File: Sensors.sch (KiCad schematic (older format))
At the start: 14 parts, among them Q20 2N7002K, Q21 2N7002K, U12 SHTC3, U13 M24C02-WDW

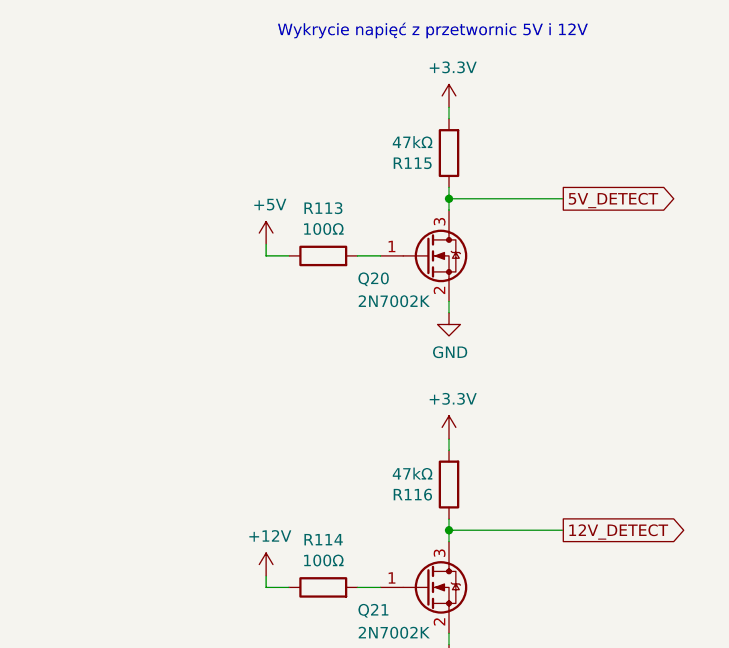
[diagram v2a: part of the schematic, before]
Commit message: Update elements value
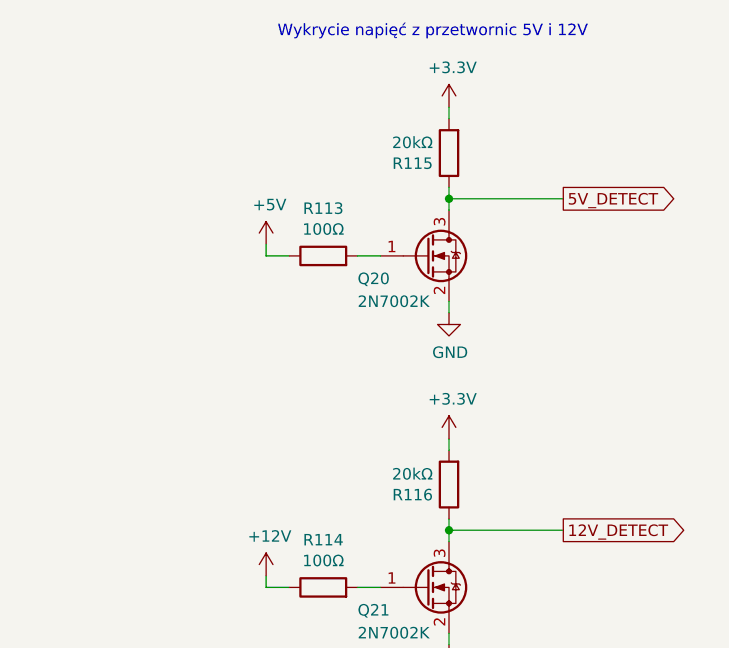
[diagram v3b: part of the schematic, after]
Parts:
- R1: Cena 0.04651 -> 0.03622
- R113, R114: Cena (none) -> 0.03185; Link (none) -> https://www.tme.eu/pl/details/smd0603-100r-1%25/rezystory-s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; Model (none) -> 0603SAF1000T5E; Opis (none) -> Rezystor: thick film; SMD; 0603; 100Ω; 0,1W; ±1%; -55÷155°C; Producent (none) -> ROYAL OHM; Typ (none) -> SMD
- R115, R116: value 47kΩ -> 20kΩ; Cena (none) -> 0.03572; Link (none) -> https://www.tme.eu/pl/details/smd0603-47k/rezystory-smd-060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; Model (none) -> 0603SAJ0473T5E; Opis (none) -> Rezystor: thick film; SMD; 0603; 47kΩ; 0,1W; ±5%; -55÷155°C; Producent (none) -> ROYAL OHM
- U13: Cena (none) -> 0.56; Link (none) -> https://pl.farnell.com/stmicroelectronics/m24c02-wdw6tp/eep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; Model (none) -> M24C02-WDW6TP; Opis (none) -> EEPROM, 2 Kbit, 256 x 8 bitów, Szeregowy I2C (2-Wire), 400 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; Producent (none) -> ST; Typ (none) -> SMD
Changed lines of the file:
@@
 AR Path="/5E1B3A8F/5E1CAE4C" Ref="R115"  Part="1"
 F 0 "R115" H 6920 1496 50  0000 L CNN
-F 1 "47kΩ" H 6920 1405 50  0000 L CNN
+F 1 "20kΩ" H 6920 1405 50  0000 L CNN
 F 2 "Resistor_SMD:R_0603_1608Metric" V 6780 1450 50  0001 C CNN
 F 3 "~" H 6850 1450 50  0001 C CNN
-F 4 "" H 6850 1450 50  0001 C CNN "Cena"
-F 5 "" H 6850 1450 50  0001 C CNN "Link"
-F 6 "" H 6850 1450 50  0001 C CNN "Model"
-F 7 "" H 6850 1450 50  0001 C CNN "Opis"
-F 8 "" H 6850 1450 50  0001 C CNN "Producent"
+F 4 "0.03572" H 6850 1450 50  0001 C CNN "Cena"
+F 5 "https://www.tme.eu/pl/details/smd0603-47k/rezystory-smd-0603/royal-ohm/0603saj0473t5e/" H 6850 1450 50  0001 C CNN "Link"
+F 6 "0603SAJ0473T5E" H 6850 1450 50  0001 C CNN "Model"
+F 7 "Rezystor: thick film; SMD; 0603; 47kΩ; 0,1W; ±5%; -55÷155°C" H 6850 1450 50  0001 C CNN "Opis"
+F 8 "ROYAL OHM" H 6850 1450 50  0001 C CNN "Producent"
 F 9 "SMD" H 6850 1450 50  0001 C CNN "Typ"
 	1    6850 1450
@@
 F 2 "Resistor_SMD:R_0603_1608Metric" V 6230 1900 50  0001 C CNN
 F 3 "~" H 6300 1900 50  0001 C CNN
+F 4 "0.03185" H 6300 1900 50  0001 C CNN "Cena"
+F 5 "https://www.tme.eu/pl/details/smd0603-100r-1%25/rezystory-smd-0603/royal-ohm/0603saf1000t5e/" H 6300 1900 50  0001 C CNN "Link"
+F 6 "0603SAF1000T5E" H 6300 1900 50  0001 C CNN "Model"
+F 7 "Rezystor: thick film; SMD; 0603; 100Ω; 0,1W; ±1%; -55÷155°C" H 6300 1900 50  0001 C CNN "Opis"
+F 8 "ROYAL OHM" H 6300 1900 50  0001 C CNN "Producent"
+F 9 "SMD" H 6300 1900 50  0001 C CNN "Typ"
 	1    6300 1900
 	0    -1   -1   0
@@
 AR Path="/5E1B3A8F/5E1DEF56" Ref="R116"  Part="1"
 F 0 "R116" H 6920 2946 50  0000 L CNN
-F 1 "47kΩ" H 6920 2855 50  0000 L CNN
+F 1 "20kΩ" H 6920 2855 50  0000 L CNN
 F 2 "Resistor_SMD:R_0603_1608Metric" V 6780 2900 50  0001 C CNN
 F 3 "~" H 6850 2900 50  0001 C CNN
-F 4 "" H 6850 2900 50  0001 C CNN "Cena"
-F 5 "" H 6850 2900 50  0001 C CNN "Link"
-F 6 "" H 6850 2900 50  0001 C CNN "Model"
-F 7 "" H 6850 2900 50  0001 C CNN "Opis"
-F 8 "" H 6850 2900 50  0001 C CNN "Producent"
+F 4 "0.03572" H 6850 2900 50  0001 C CNN "Cena"
+F 5 "https://www.tme.eu/pl/details/smd0603-47k/rezystory-smd-0603/royal-ohm/0603saj0473t5e/" H 6850 2900 50  0001 C CNN "Link"
+F 6 "0603SAJ0473T5E" H 6850 2900 50  0001 C CNN "Model"
+F 7 "Rezystor: thick film; SMD; 0603; 47kΩ; 0,1W; ±5%; -55÷155°C" H 6850 2900 50  0001 C CNN "Opis"
+F 8 "ROYAL OHM" H 6850 2900 50  0001 C CNN "Producent"
 F 9 "SMD" H 6850 2900 50  0001 C CNN "Typ"
 	1    6850 2900
@@
 F 2 "Resistor_SMD:R_0603_1608Metric" V 6230 3350 50  0001 C CNN
 F 3 "~" H 6300 3350 50  0001 C CNN
+F 4 "0.03185" H 6300 3350 50  0001 C CNN "Cena"
+F 5 "https://www.tme.eu/pl/details/smd0603-100r-1%25/rezystory-smd-0603/royal-ohm/0603saf1000t5e/" H 6300 3350 50  0001 C CNN "Link"
+F 6 "0603SAF1000T5E" H 6300 3350 50  0001 C CNN "Model"
+F 7 "Rezystor: thick film; SMD; 0603; 100Ω; 0,1W; ±1%; -55÷155°C" H 6300 3350 50  0001 C CNN "Opis"
+F 8 "ROYAL OHM" H 6300 3350 50  0001 C CNN "Producent"
+F 9 "SMD" H 6300 3350 50  0001 C CNN "Typ"
 	1    6300 3350
 	0    -1   -1   0
@@
 F 2 "Package_SO:TSSOP-8_4.4x3mm_P0.65mm" H 3550 4200 50  0001 C CNN
 F 3 "http://www.st.com/content/ccc/resource/technical/document/datasheet/b0/d8/50/40/5a/85/49/6f/DM00071904.pdf/files/DM00071904.pdf/jcr:content/translations/en.DM00071904.pdf" H 3600 3350 50  0001 C CNN
+F 4 "0.56" H 3550 3850 50  0001 C CNN "Cena"
+F 5 "https://pl.farnell.com/stmicroelectronics/m24c02-wdw6tp/eeprom-2kbit-i2c-400khz-tssop/dp/2849956RL" H 3550 3850 50  0001 C CNN "Link"
+F 6 "M24C02-WDW6TP" H 3550 3850 50  0001 C CNN "Model"
+F 7 "EEPROM, 2 Kbit, 256 x 8 bitów, Szeregowy I2C (2-Wire), 400 kHz, TSSOP, 8 piny/-ów" H 3550 3850 50  0001 C CNN "Opis"
+F 8 "ST" H 3550 3850 50  0001 C CNN "Producent"
+F 9 "SMD" H 3550 3850 50  0001 C CNN "Typ"
 	1    3550 3850
 	1    0    0    -1
@@
 F 2 "Resistor_SMD:R_0603_1608Metric" V 4680 3700 50  0001 C CNN
 F 3 "~" H 4750 3700 50  0001 C CNN
-F 4 "0.04651" H 4750 3700 50  0001 C CNN "Cena"
+F 4 "0.03622" H 4750 3700 50  0001 C CNN "Cena"
 F 5 "SMD" H 4750 3700 50  0001 C CNN "Typ"
 	1    4750 3700

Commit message: Updated BOM on schematics
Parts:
- C83, C95: Cena 0.05982 -> 0.07894; Dielektryk (none) -> X7R; Link (none) -> https://www.tme.eu/pl/details/cl10b104kb8nnnc/kondensatory-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; Model CL10B104KB8NNNC -> CL10B104KB8NNNC; Opis (none) -> Kondensator: ceramiczny; MLCC; 100nF; 50V; X7R; ±10%; SMD; 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
- R111: Link (none) -> https://www.tme.eu/pl/details/0603saj0000t5e/rezystory-smd-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; Model (none) -> 0603SAJ0000T5E; Opis (none) -> Rezystor: thick film; SMD; 0603; 0Ω; 0,1W; ±5%; -55÷155°C; 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; Producent (none) -> ROYAL OHM
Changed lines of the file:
@@
 F 2 "Capacitor_SMD:C_0603_1608Metric" H 3938 2300 50  0001 C CNN
 F 3 "~" H 3900 2450 50  0001 C CNN
-F 4 "0.05982" H 3900 2450 50  0001 C CNN "Cena"
-F 5 "CL10B104KB8NNNC " H 3900 2450 50  0001 C CNN "Model"
+F 4 "0.07894" H 3900 2450 50  0001 C CNN "Cena"
+F 5 "CL10B104KB8NNNC" H 3900 2450 50  0001 C CNN "Model"
 F 6 "50V" H 3900 2450 50  0001 C CNN "Napięcie"
 F 7 "SAMSUNG" H 3900 2450 50  0001 C CNN "Producent"
 F 8 "10%" H 3900 2450 50  0001 C CNN "Tolerancja"
 F 9 "SMD" H 3900 2450 50  0001 C CNN "Typ"
+F 10 "X7R" H 3900 2450 50  0001 C CNN "Dielektryk"
+F 11 "https://www.tme.eu/pl/details/cl10b104kb8nnnc/kondensatory-mlcc-smd-0603/samsung/" H 3900 2450 50  0001 C CNN "Link"
+F 12 "Kondensator: ceramiczny; MLCC; 100nF; 50V; X7R; ±10%; SMD; 0603" H 3900 2450 50  0001 C CNN "Opis"
 	1    3900 2450
 	1    0    0    -1
@@
 F 4 "0.04651" H 2500 2500 50  0001 C CNN "Cena"
 F 5 "SMD" H 2500 2500 50  0001 C CNN "Typ"
+F 6 "https://www.tme.eu/pl/details/0603saj0000t5e/rezystory-smd-0603/royal-ohm/" H 2500 2500 50  0001 C CNN "Link"
+F 7 "0603SAJ0000T5E" H 2500 2500 50  0001 C CNN "Model"
+F 8 "Rezystor: thick film; SMD; 0603; 0Ω; 0,1W; ±5%; -55÷155°C; 400ppm/°C" H 2500 2500 50  0001 C CNN "Opis"
+F 9 "ROYAL OHM" H 2500 2500 50  0001 C CNN "Producent"
 	1    2500 2500
 	0    -1   -1   0
@@
 F 2 "Capacitor_SMD:C_0603_1608Metric" H 2988 3500 50  0001 C CNN
 F 3 "~" H 2950 3650 50  0001 C CNN
-F 4 "0.05982" H 2950 3650 50  0001 C CNN "Cena"
-F 5 "CL10B104KB8NNNC " H 2950 3650 50  0001 C CNN "Model"
+F 4 "0.07894" H 2950 3650 50  0001 C CNN "Cena"
+F 5 "CL10B104KB8NNNC" H 2950 3650 50  0001 C CNN "Model"
 F 6 "50V" H 2950 3650 50  0001 C CNN "Napięcie"
 F 7 "SAMSUNG" H 2950 3650 50  0001 C CNN "Producent"
 F 8 "10%" H 2950 3650 50  0001 C CNN "Tolerancja"
 F 9 "SMD" H 2950 3650 50  0001 C CNN "Typ"
+F 10 "X7R" H 2950 3650 50  0001 C CNN "Dielektryk"
+F 11 "https://www.tme.eu/pl/details/cl10b104kb8nnnc/kondensatory-mlcc-smd-0603/samsung/" H 2950 3650 50  0001 C CNN "Link"
+F 12 "Kondensator: ceramiczny; MLCC; 100nF; 50V; X7R; ±10%; SMD; 0603" H 2950 3650 50  0001 C CNN "Opis"
 	1    2950 3650
 	-1   0    0    1
